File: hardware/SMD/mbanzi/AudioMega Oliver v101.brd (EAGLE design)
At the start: 58 x 49 mm, 72 parts, among them Q1 BC846ASMD, Q2 BC846ASMD, Q3 BC846ASMD, Q4 2N7002, Q5 BC846ASMD, Q6 BC846ASMD, U1 REG1117-5, U2 REG1117-3.3, U3 ATMEGA328-AU, U4 LM386M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

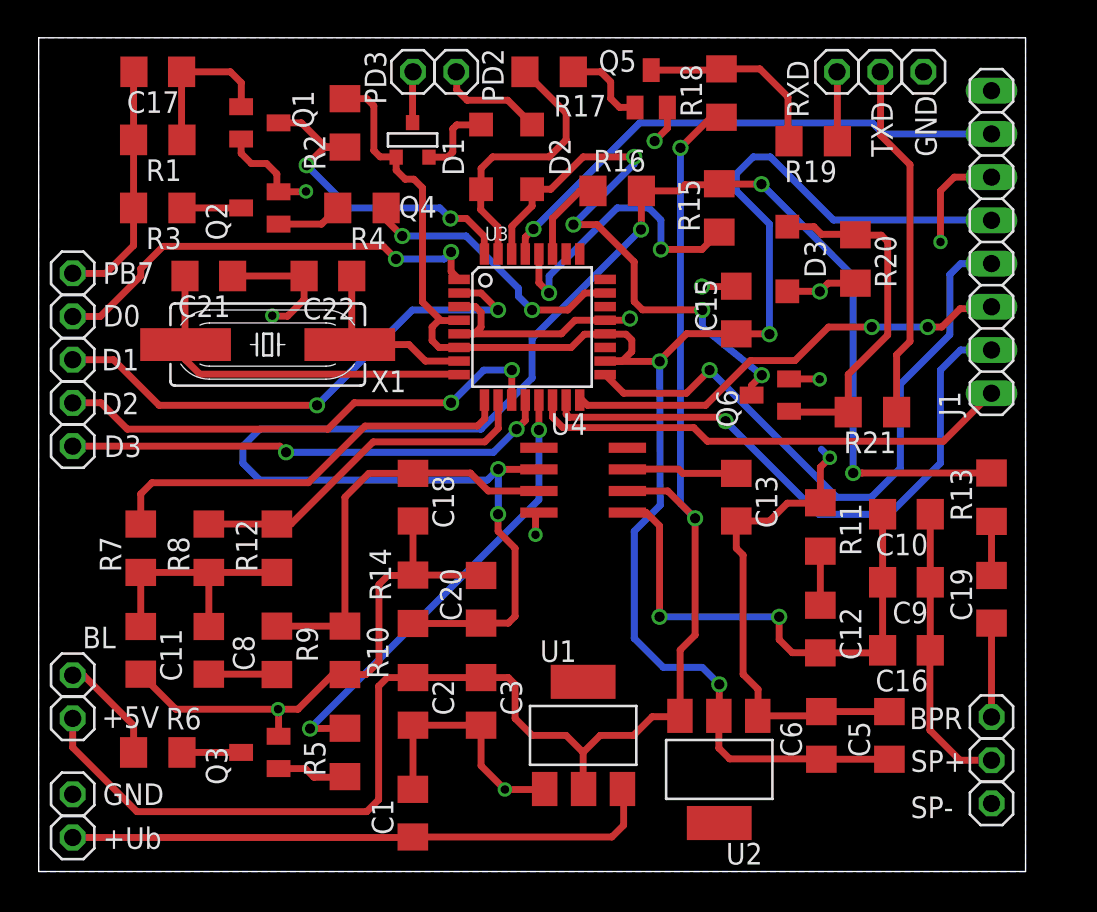
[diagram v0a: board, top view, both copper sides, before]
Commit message: Added Eagle 6.3.0 files for all my versions of the designs
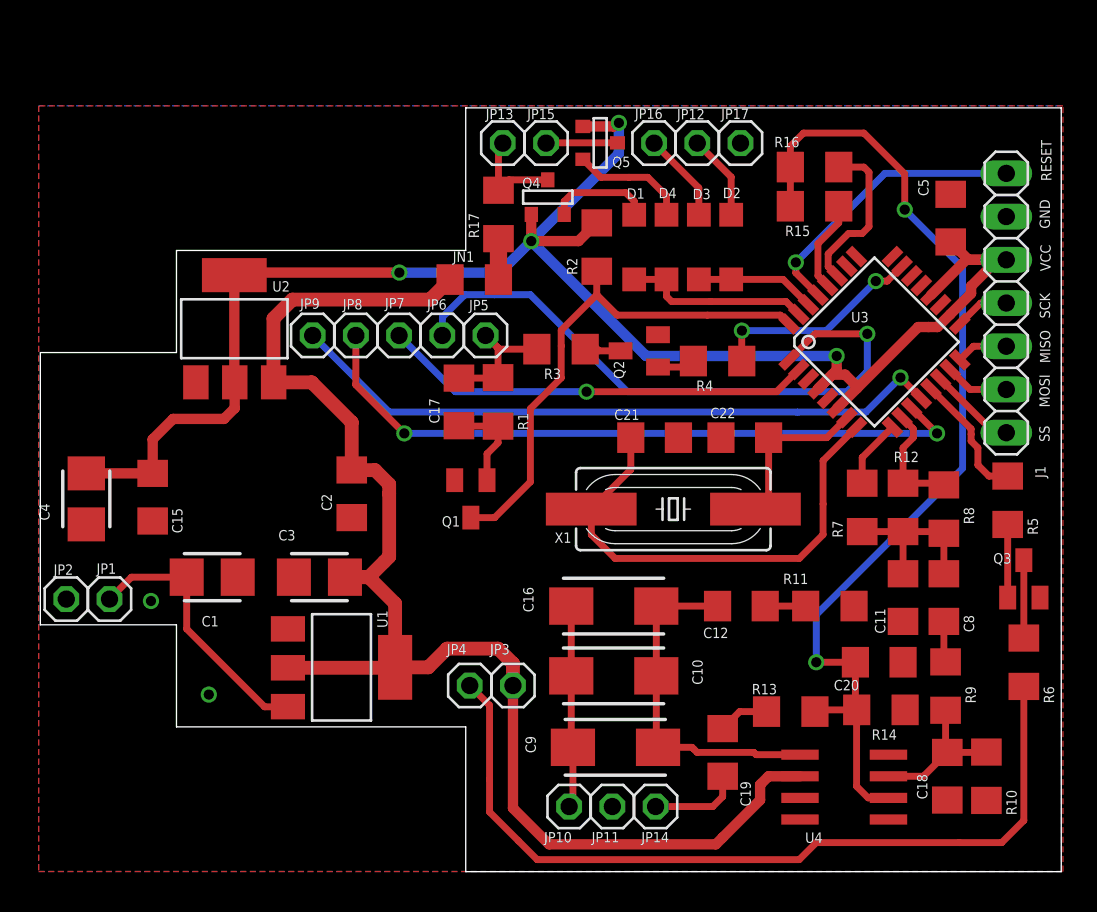
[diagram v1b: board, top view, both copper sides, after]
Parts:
- removed C13: 100nF, resistor:C1206
- removed C6: 10uF, resistor:C1206
- removed Q6: BC846ASMD, transistor-npn:SOT23
- removed R18: 2k2, resistor:R1206
- removed R19: 470, resistor:R1206
- removed R20, R21: 10k, resistor:R1206
- added C4: 10uF, resistor:CT3528
- added D4: BAT42, diode:SOD123
- added JN1: 0, resistor:R1206
- C1, C3: device resistor:C1206 -> resistor:CT3528
- C10, C16, C9: device resistor:C1206 -> resistor:CT6032
- C18: value 10nF -> 4n7
- C20: value 47nF -> 22nF
- J1: device pinhead:1X08 -> pinhead:1X07
- JP13: value PD3 -> RXD-TTL5v
- JP15: value RXD -> PD3
- JP16: value TXD -> TXD-TTL5v
- JP3: value +5V -> BL+ (+5v)
- JP4: value BL -> BL-
- Q5: value BC846ASMD -> 2N7002; device transistor-npn:SOT23 -> zetex:SOT-23
- R17: value 22k -> 1k
- moved R6 51.2 mm to (57.9, 12.3), turned to 90 degrees
- moved Q3 46.0 mm to (57.9, 17.2), turned to 0 degrees
- moved C11 44.9 mm to (50.8, 16.1)
- moved C8 43.3 mm to (53.2, 16.1)
- moved R8 43.3 mm to (53.2, 21.3)
- moved R7 42.5 mm to (48.4, 21.4)
- moved R5 41.7 mm to (57.0, 21.8)
- moved R9 39.4 mm to (53.3, 10.9), turned to 90 degrees
- moved U2 38.5 mm to (11.5, 31.9), turned to 0 degrees
- moved R10 38.4 mm to (55.7, 5.60)
- moved R12 36.9 mm to (50.8, 21.4)
- moved C15 36.0 mm to (6.70, 22.0), turned to 270 degrees
- moved C18 35.4 mm to (53.4, 5.60)
- moved C5 30.6 mm to (53.6, 38.4)
- moved R14 28.3 mm to (49.5, 9.50), turned to 180 degrees
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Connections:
- removed net N$14: C13.1, U4.7
- removed net N$40: D3.C, Q6.1, R20.1, R21.2
- removed net N$43: Q5.3, R18.2, R19.2
- removed net N$44: Q5.1, R17.2
- new net N$2: D4.A, Q5.2
- new net N$22: JN1.1, R17.1
- net +3V3: now also C4.+, Q5.3, U2.4; no longer C6.1
- net +5V: now also C3.+, JN1.2, U1.4; no longer C3.1, R18.1
- net GND: now also C1.-, C3.-, C4.-; no longer C1.2, C13.2, C3.2, C6.2, D3.A, Q5.2, Q6.2, R20.2
- net N$15: now also C10.-, C16.-, C9.-; no longer C10.1, C16.1, C9.1
- net N$17: now also C10.+, C16.+, C9.+; no longer C10.2, C16.2, C9.2
- net N$32: now also C1.+; no longer C1.1
- net N$37: now also D3.C; no longer R21.1
- net N$38: now also Q5.1; no longer R19.1
- net N$41: now also R17.2
- net N$42: now also D3.A; no longer Q6.3
- net N$46: now also D4.C; no longer R17.1
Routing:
- net GND: track 121.1 -> 0.00 mm, vias 12 -> 2
- net N$29: track 6.39 -> 49.3 mm
- net VOL_B: track 101.2 -> 59.5 mm, vias 5 -> 2
- net N$5: track 37.5 -> 3.24 mm, vias 1 -> 0
- net N$3: track 35.5 -> 3.78 mm, vias 1 -> 0
- net N$42: track 34.7 -> 7.05 mm, vias 4 -> 0
- net N$4: track 26.8 -> 3.06 mm, vias 2 -> 0
- net N$21: track 28.6 -> 5.17 mm
- net N$27: track 24.9 -> 4.02 mm
- net N$40: track 20.7 -> 0.00 mm
- net N$34: track 26.9 -> 7.65 mm, vias 2 -> 0
- net N$32: track 34.8 -> 16.0 mm
- net N$37: track 21.1 -> 5.30 mm
- net N$18: track 24.0 -> 8.87 mm
- net N$6: track 31.4 -> 17.0 mm
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- added copper zone on layer 1, net GND
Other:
- board size 58 x 49 mm -> 60 x 44.9 mm
- board text added: "MISO"
- board text added: "MOSI"
- board text added: "RESET"
- board text added: "SCK"
- board text added: "SS"
- board text added: "VCC"
- board text removed: "+5V"
- board text removed: "+Ub"
- board text removed: "AudioMega v1.0"
- board text removed: "BL"
- board text removed: "BPR"
- board text removed: "D0"
- board text removed: "D1"
- board text removed: "D2"
- board text removed: "D3"
- board text removed: "PB7"
- board text removed: "PD2"
- board text removed: "PD3"
- board text removed: "RXD"
- board text removed: "SP+"
- board text removed: "SP-"
- board text removed: "TXD"
